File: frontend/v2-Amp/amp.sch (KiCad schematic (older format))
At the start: 70 parts, among them K1 HK4100, P1 Antenna, P2 CONN_02X06, P3 TX Power Tap, P4 TX-IN, P5 RX IN, P6 12-13.8v, Q1 PZT2222A, Q2 RD16HHF1, T1 OUT_TRANSF, T2 BN-43-2402, U1 LP2951-50D

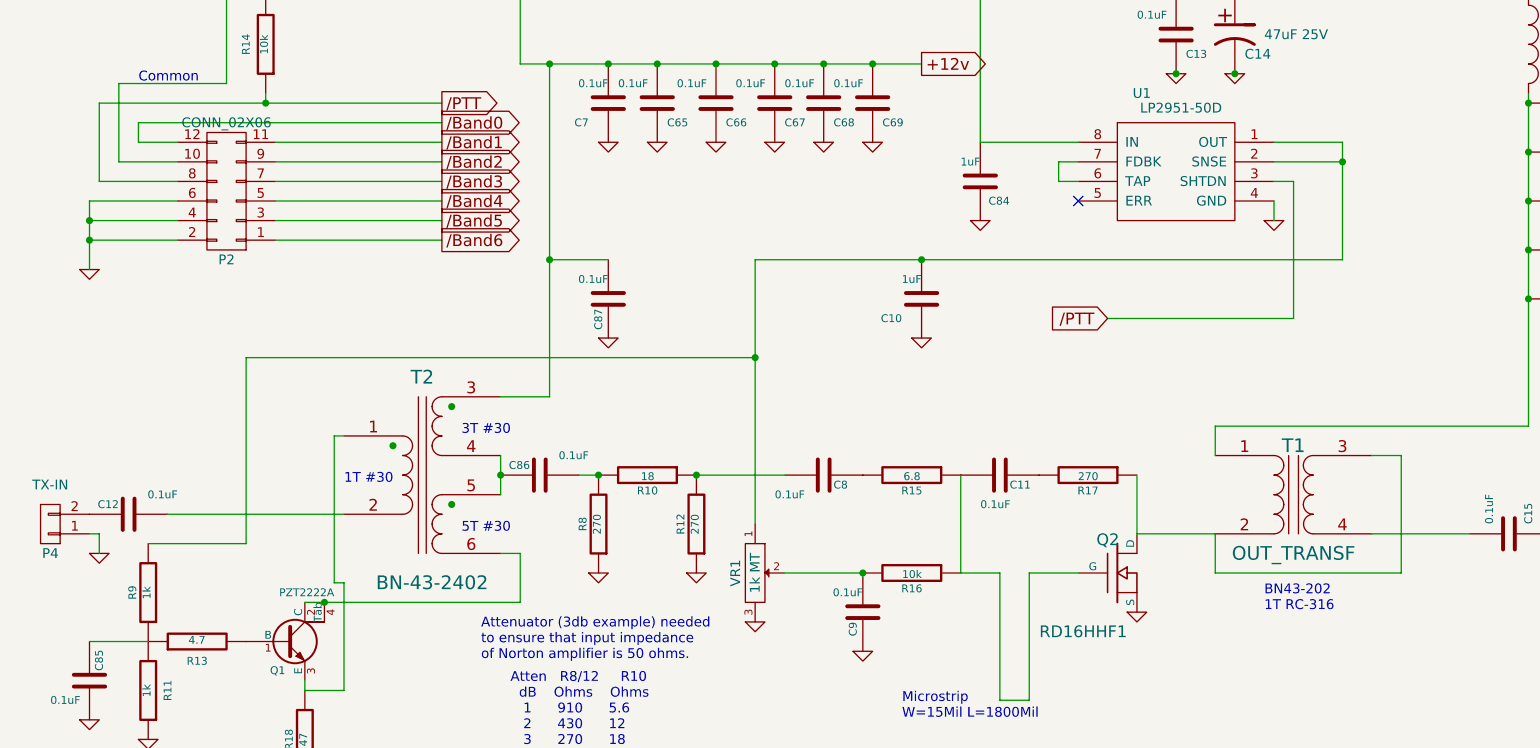
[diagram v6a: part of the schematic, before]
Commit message: Updates for bias and 40/60 filter
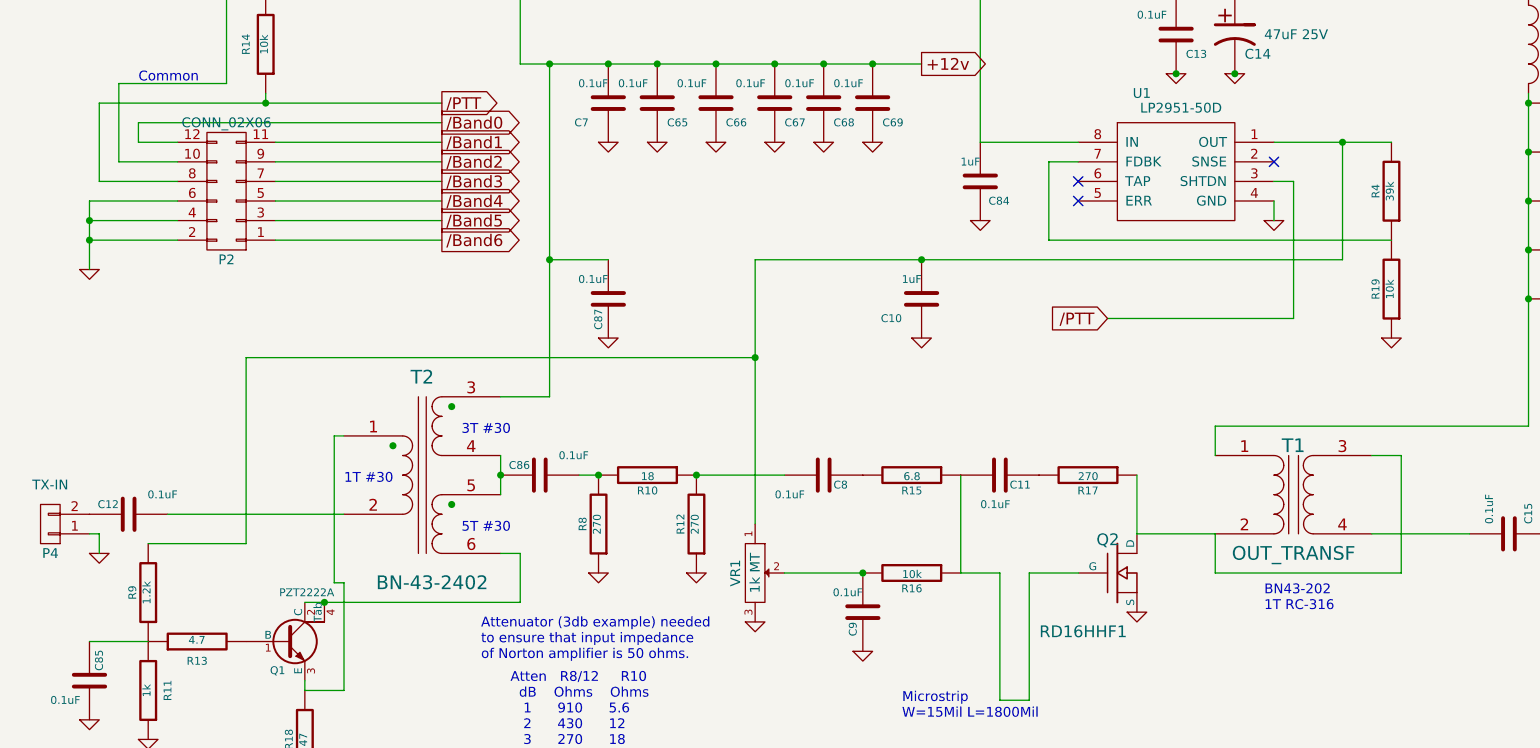
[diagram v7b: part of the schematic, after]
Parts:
- added R19: 10k, Resistors_SMD:R_0805_HandSoldering, symbol R
- added R4: 39k, Resistors_SMD:R_0805_HandSoldering, symbol R
- R9: value 1k -> 1.2k
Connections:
- net GND: now also R19.1
- net at C10.2, R9.2, U1.1 (OUT)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: now also R4.2; no longer U1.2 (SNSE)
- net at U1.6 (TAP): no longer U1.7 (FDBK)
- new net: R19.2, R4.1, U1.7 (FDBK)
- no-connect marks 3 -> 5
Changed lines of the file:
@@
 $EndComp
 $Comp
-L GND #PWR01
+L GND #PWR26
 U 1 1 547BF2DF
 P 6800 4400
-F 0 "#PWR01" H 6800 4400 30  0001 C CNN
+F 0 "#PWR26" H 6800 4400 30  0001 C CNN
 F 1 "GND" H 6800 4330 30  0001 C CNN
 F 2 "" H 6800 4400 60  0000 C CNN
@@
 $EndComp
 $Comp
-L GND #PWR02
+L GND #PWR28
 U 1 1 5487313F
 P 7300 1650
-F 0 "#PWR02" H 7300 1650 30  0001 C CNN
+F 0 "#PWR28" H 7300 1650 30  0001 C CNN
 F 1 "GND" H 7300 1580 30  0001 C CNN
 F 2 "" H 7300 1650 60  0000 C CNN
@@
 $EndComp
 $Comp
-L GND #PWR03
+L GND #PWR22
 U 1 1 54AEA6C8
 P 5400 4600
-F 0 "#PWR03" H 5400 4600 30  0001 C CNN
+F 0 "#PWR22" H 5400 4600 30  0001 C CNN
 F 1 "GND" H 5400 4530 30  0001 C CNN
 F 2 "" H 5400 4600 60  0000 C CNN
@@
 $EndComp
 $Comp
-L GND #PWR04
+L GND #PWR19
 U 1 1 54AEA705
 P 4850 4450
-F 0 "#PWR04" H 4850 4450 30  0001 C CNN
+F 0 "#PWR19" H 4850 4450 30  0001 C CNN
 F 1 "GND" H 4850 4380 30  0001 C CNN
 F 2 "" H 4850 4450 60  0000 C CNN
@@
 $EndComp
 $Comp
-L GND #PWR05
+L GND #PWR32
 U 1 1 54AF012A
 P 9400 2900
-F 0 "#PWR05" H 9400 2900 30  0001 C CNN
+F 0 "#PWR32" H 9400 2900 30  0001 C CNN
 F 1 "GND" H 9400 2830 30  0001 C CNN
 F 2 "" H 9400 2900 60  0000 C CNN
@@
 $EndComp
 $Comp
-L GND #PWR06
+L GND #PWR24
 U 1 1 54B3D8F0
 P 5700 3000
-F 0 "#PWR06" H 5700 3000 30  0001 C CNN
+F 0 "#PWR24" H 5700 3000 30  0001 C CNN
 F 1 "GND" H 5700 2930 30  0001 C CNN
 F 2 "" H 5700 3000 60  0000 C CNN
@@
 $EndComp
 $Comp
-L GND #PWR07
+L GND #PWR27
 U 1 1 54D83616
 P 7000 1650
-F 0 "#PWR07" H 7000 1650 30  0001 C CNN
+F 0 "#PWR27" H 7000 1650 30  0001 C CNN
 F 1 "GND" H 7000 1580 30  0001 C CNN
 F 2 "" H 7000 1650 60  0000 C CNN
@@
 $EndComp
 $Comp
-L GND #PWR08
+L GND #PWR31
 U 1 1 550ED567
 P 8350 850
-F 0 "#PWR08" H 8350 850 30  0001 C CNN
+F 0 "#PWR31" H 8350 850 30  0001 C CNN
 F 1 "GND" H 8350 780 30  0001 C CNN
 F 2 "" H 8350 850 60  0000 C CNN
@@
 $EndComp
 $Comp
-L GND #PWR09
+L GND #PWR11
 U 1 1 55CE57E8
 P 4050 4200
-F 0 "#PWR09" H 4050 4200 30  0001 C CNN
+F 0 "#PWR11" H 4050 4200 30  0001 C CNN
 F 1 "GND" H 4050 4130 30  0001 C CNN
 F 2 "" H 4050 4200 60  0000 C CNN
@@
 NoConn ~ 6000 5950
 $Comp
-L GND #PWR010
+L GND #PWR1
 U 1 1 55CEE6B0
 P 1250 6450
-F 0 "#PWR010" H 1250 6450 30  0001 C CNN
+F 0 "#PWR1" H 1250 6450 30  0001 C CNN
 F 1 "GND" H 1250 6380 30  0001 C CNN
 F 2 "" H 1250 6450 60  0000 C CNN
@@
 Connection ~ 7000 1250
 $Comp
-L GND #PWR011
+L GND #PWR2
 U 1 1 55CF36AA
 P 1450 2650
-F 0 "#PWR011" H 1450 2650 30  0001 C CNN
+F 0 "#PWR2" H 1450 2650 30  0001 C CNN
 F 1 "GND" H 1450 2580 30  0001 C CNN
 F 2 "" H 1450 2650 60  0000 C CNN
@@
 $EndComp
 $Comp
-L GND #PWR012
+L GND #PWR15
 U 1 1 55CF8B50
 P 4350 2000
-F 0 "#PWR012" H 4350 2000 30  0001 C CNN
+F 0 "#PWR15" H 4350 2000 30  0001 C CNN
 F 1 "GND" H 4350 1930 30  0001 C CNN
 F 2 "" H 4350 2000 60  0000 C CNN
@@
 Connection ~ 3700 7700
 $Comp
-L GND #PWR013
+L GND #PWR10
 U 1 1 55CFFA7F
 P 3700 7800
-F 0 "#PWR013" H 3700 7800 30  0001 C CNN
+F 0 "#PWR10" H 3700 7800 30  0001 C CNN
 F 1 "GND" H 3700 7730 30  0001 C CNN
 F 2 "" H 3700 7800 60  0000 C CNN
@@
 	1500 4000 1500 4100
 $Comp
-L GND #PWR014
+L GND #PWR4
 U 1 1 55D1DC89
 P 1500 4100
-F 0 "#PWR014" H 1500 4100 30  0001 C CNN
+F 0 "#PWR4" H 1500 4100 30  0001 C CNN
 F 1 "GND" H 1500 4030 30  0001 C CNN
 F 2 "" H 1500 4100 60  0000 C CNN
@@
 $EndComp
 $Comp
-L GND #PWR015
+L GND #PWR16
 U 1 1 55D1DDBB
 P 4550 4200
-F 0 "#PWR015" H 4550 4200 30  0001 C CNN
+F 0 "#PWR16" H 4550 4200 30  0001 C CNN
 F 1 "GND" H 4550 4130 30  0001 C CNN
 F 2 "" H 4550 4200 60  0000 C CNN
@@
 	1950 5500 1950 5600
 $Comp
-L GND #PWR016
+L GND #PWR6
 U 1 1 55D1EA74
 P 1950 5600
-F 0 "#PWR016" H 1950 5600 30  0001 C CNN
+F 0 "#PWR6" H 1950 5600 30  0001 C CNN
 F 1 "GND" H 1950 5530 30  0001 C CNN
 F 2 "" H 1950 5600 60  0000 C CNN
@@
 $EndComp
 $Comp
-L GND #PWR017
+L GND #PWR25
 U 1 1 55DF08F0
 P 6000 2400
-F 0 "#PWR017" H 6000 2400 30  0001 C CNN
+F 0 "#PWR25" H 6000 2400 30  0001 C CNN
 F 1 "GND" H 6000 2330 30  0001 C CNN
 F 2 "" H 6000 2400 60  0000 C CNN
@@
 $EndComp
 $Comp
-L GND #PWR018
+L GND #PWR17
 U 1 1 55DF0936
 P 4650 2000
-F 0 "#PWR018" H 4650 2000 30  0001 C CNN
+F 0 "#PWR17" H 4650 2000 30  0001 C CNN
 F 1 "GND" H 4650 1930 30  0001 C CNN
 F 2 "" H 4650 2000 60  0000 C CNN
@@
 $EndComp
 $Comp
-L GND #PWR019
+L GND #PWR20
 U 1 1 55DF097C
 P 4950 2000
-F 0 "#PWR019" H 4950 2000 30  0001 C CNN
+F 0 "#PWR20" H 4950 2000 30  0001 C CNN
 F 1 "GND" H 4950 1930 30  0001 C CNN
 F 2 "" H 4950 2000 60  0000 C CNN
@@
 $EndComp
 $Comp
-L GND #PWR020
+L GND #PWR21
 U 1 1 55DF09C2
 P 5200 2000
-F 0 "#PWR020" H 5200 2000 30  0001 C CNN
+F 0 "#PWR21" H 5200 2000 30  0001 C CNN
 F 1 "GND" H 5200 1930 30  0001 C CNN
 F 2 "" H 5200 2000 60  0000 C CNN
@@
 $EndComp
 $Comp
-L GND #PWR021
+L GND #PWR23
 U 1 1 55DF1874
 P 5450 2000
-F 0 "#PWR021" H 5450 2000 30  0001 C CNN
+F 0 "#PWR23" H 5450 2000 30  0001 C CNN
 F 1 "GND" H 5450 1930 30  0001 C CNN
 F 2 "" H 5450 2000 60  0000 C CNN
@@
 +12v
 $Comp
-L GND #PWR022
+L GND #PWR13
 U 1 1 55E26F7C
 P 4100 2000
-F 0 "#PWR022" H 4100 2000 30  0001 C CNN
+F 0 "#PWR13" H 4100 2000 30  0001 C CNN
 F 1 "GND" H 4100 1930 30  0001 C CNN
 F 2 "" H 4100 2000 60  0000 C CNN
@@
 	7850 2600 7850 2000
 Wire Wire Line
-	7850 2000 7500 2000
+	7500 2000 8100 2000
 Wire Wire Line
 	6500 2000 6000 2000
@@
 	7600 2200 7600 2900
 Wire Wire Line
-	6500 2200 6400 2200
-Wire Wire Line
-	6400 2200 6400 2100
-Wire Wire Line
-	6400 2100 6500 2100
+	6350 2100 6500 2100
 NoConn ~ 6500 2300
 Wire Wire Line
-	7500 2100 7850 2100
-Connection ~ 7850 2100
-Wire Wire Line
 	7500 2300 7500 2400
 $Comp
-L GND #PWR023
+L GND #PWR29
 U 1 1 55E317B4
 P 7500 2400
-F 0 "#PWR023" H 7500 2400 30  0001 C CNN
+F 0 "#PWR29" H 7500 2400 30  0001 C CNN
 F 1 "GND" H 7500 2330 30  0001 C CNN
 F 2 "" H 7500 2400 60  0000 C CNN
@@
 P 1750 4300
 F 0 "R9" V 1830 4300 40  0000 C CNN
-F 1 "1k" V 1757 4301 40  0000 C CNN
+F 1 "1.2k" V 1757 4301 40  0000 C CNN
 F 2 "Resistors_SMD:R_0805_HandSoldering" V 1680 4300 30  0001 C CNN
 F 3 "" H 1750 4300 30  0000 C CNN
@@
 Connection ~ 3800 2600
 $Comp
-L GND #PWR024
+L GND #PWR14
 U 1 1 55E478DE
 P 4100 3000
-F 0 "#PWR024" H 4100 3000 30  0001 C CNN
+F 0 "#PWR14" H 4100 3000 30  0001 C CNN
 F 1 "GND" H 4100 2930 30  0001 C CNN
 F 2 "" H 4100 3000 60  0000 C CNN
@@
 $EndComp
 $Comp
-L GND #PWR025
+L GND #PWR5
 U 1 1 55E488C1
 P 1750 5050
-F 0 "#PWR025" H 1750 5050 30  0001 C CNN
+F 0 "#PWR5" H 1750 5050 30  0001 C CNN
 F 1 "GND" H 1750 4980 30  0001 C CNN
 F 2 "" H 1750 5050 60  0000 C CNN
@@
 $EndComp
 $Comp
-L GND #PWR026
+L GND #PWR7
 U 1 1 55E48911
 P 2550 5300
-F 0 "#PWR026" H 2550 5300 30  0001 C CNN
+F 0 "#PWR7" H 2550 5300 30  0001 C CNN
 F 1 "GND" H 2550 5230 30  0001 C CNN
 F 2 "" H 2550 5300 60  0000 C CNN
@@
 $EndComp
 $Comp
-L GND #PWR027
+L GND #PWR3
 U 1 1 55EA100D
 P 1450 4950
-F 0 "#PWR027" H 1450 4950 30  0001 C CNN
+F 0 "#PWR3" H 1450 4950 30  0001 C CNN
 F 1 "GND" H 1450 4880 30  0001 C CNN
 F 2 "" H 1450 4950 60  0000 C CNN
@@
 $EndComp
 $Comp
-L GND #PWR028
+L GND #PWR8
 U 1 1 560EC10F
 P 2850 6650
-F 0 "#PWR028" H 2850 6650 30  0001 C CNN
+F 0 "#PWR8" H 2850 6650 30  0001 C CNN
 F 1 "GND" H 2850 6580 30  0001 C CNN
 F 2 "" H 2850 6650 60  0000 C CNN
@@
 $EndComp
 $Comp
-L GND #PWR029
+L GND #PWR9
 U 1 1 560EC115
 P 3450 6650
-F 0 "#PWR029" H 3450 6650 30  0001 C CNN
+F 0 "#PWR9" H 3450 6650 30  0001 C CNN
 F 1 "GND" H 3450 6580 30  0001 C CNN
 F 2 "" H 3450 6650 60  0000 C CNN
@@
 $EndComp
 $Comp
-L GND #PWR030
+L GND #PWR12
 U 1 1 560EC11B
 P 4050 6650
-F 0 "#PWR030" H 4050 6650 30  0001 C CNN
+F 0 "#PWR12" H 4050 6650 30  0001 C CNN
 F 1 "GND" H 4050 6580 30  0001 C CNN
 F 2 "" H 4050 6650 60  0000 C CNN
@@
 	4650 5950 4650 6250
 $Comp
-L GND #PWR031
+L GND #PWR18
 U 1 1 560EC150
 P 4650 6650
-F 0 "#PWR031" H 4650 6650 30  0001 C CNN
+F 0 "#PWR18" H 4650 6650 30  0001 C CNN
 F 1 "GND" H 4650 6580 30  0001 C CNN
 F 2 "" H 4650 6650 60  0000 C CNN
@@
 Wire Wire Line
 	4650 6250 5000 6250
+$Comp
+L R R4
+U 1 1 5628F05D
+P 8100 2250
+F 0 "R4" V 8180 2250 40  0000 C CNN
+F 1 "39k" V 8107 2251 40  0000 C CNN
+F 2 "Resistors_SMD:R_0805_HandSoldering" V 8030 2250 30  0001 C CNN
+F 3 "" H 8100 2250 30  0000 C CNN
+	1    8100 2250
+	-1   0    0    1
+$EndComp
+$Comp
+L R R19
+U 1 1 5628F10E
+P 8100 2750
+F 0 "R19" V 8180 2750 40  0000 C CNN
+F 1 "10k" V 8107 2751 40  0000 C CNN
+F 2 "Resistors_SMD:R_0805_HandSoldering" V 8030 2750 30  0001 C CNN
+F 3 "" H 8100 2750 30  0000 C CNN
+	1    8100 2750
+	-1   0    0    1
+$EndComp
+$Comp
+L GND #PWR30
+U 1 1 5628F45A
+P 8100 3000
+F 0 "#PWR30" H 8100 3000 30  0001 C CNN
+F 1 "GND" H 8100 2930 30  0001 C CNN
+F 2 "" H 8100 3000 60  0000 C CNN
+F 3 "" H 8100 3000 60  0000 C CNN
+	1    8100 3000
+	1    0    0    -1
+$EndComp
+Wire Wire Line
+	8100 2500 6350 2500
+Wire Wire Line
+	6350 2500 6350 2100
+Connection ~ 7850 2000
+NoConn ~ 7500 2100
+NoConn ~ 6500 2200
 $EndSCHEMATC
